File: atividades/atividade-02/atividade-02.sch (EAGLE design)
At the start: 10 parts, among them IC1 LM358N, Q1 BS170

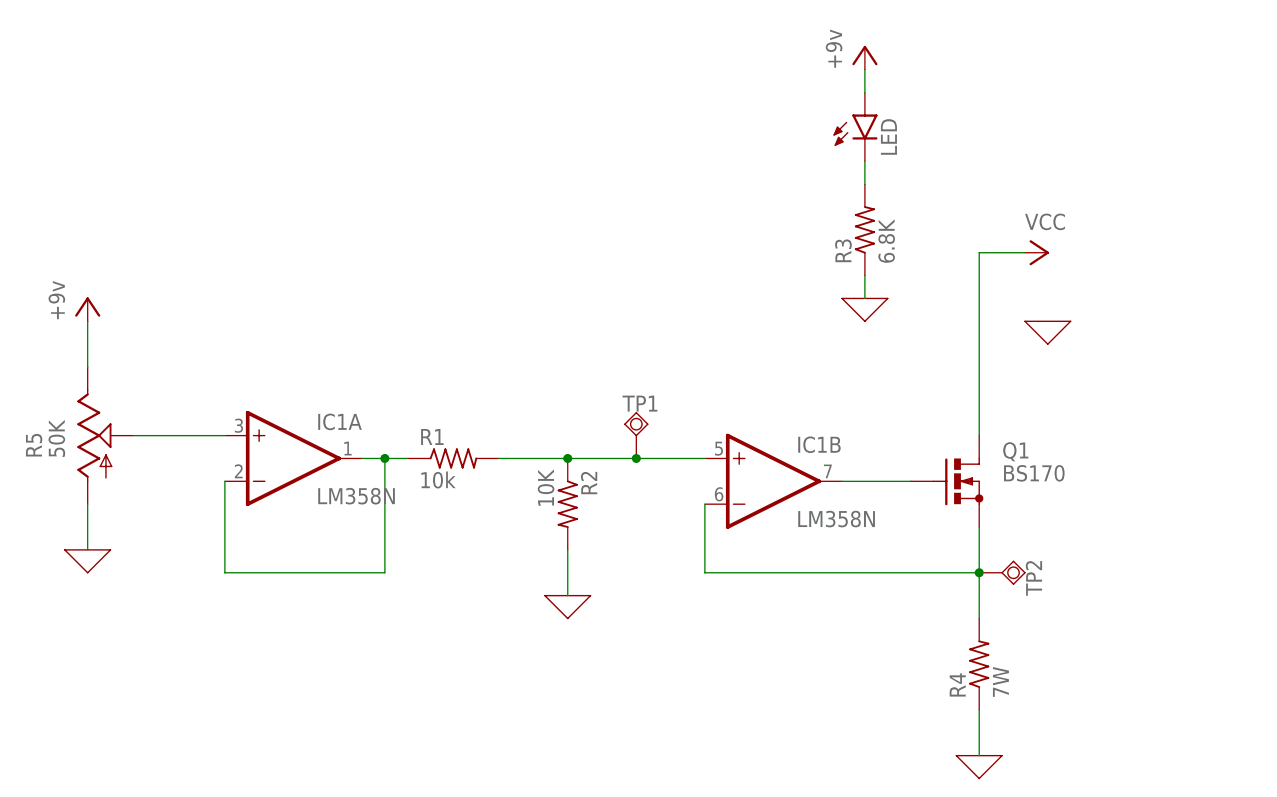
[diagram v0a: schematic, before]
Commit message: renomeando componentes
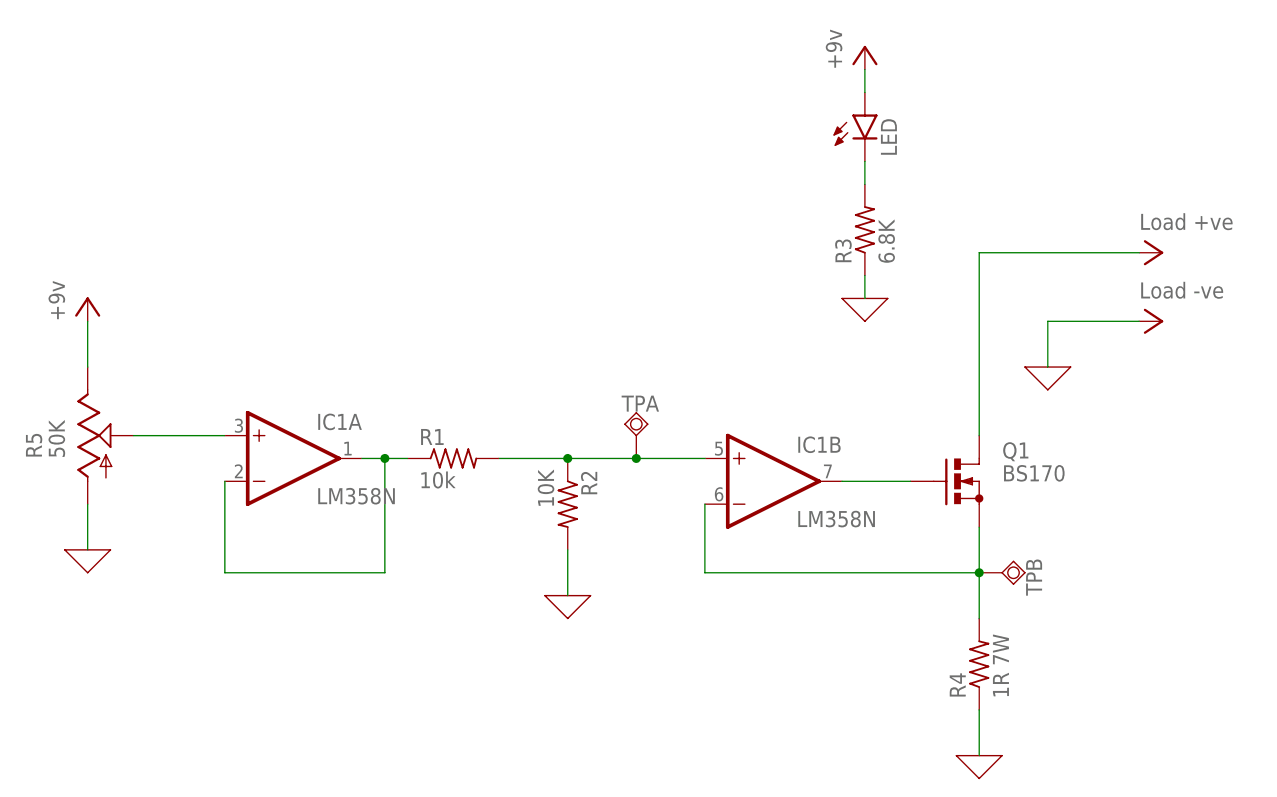
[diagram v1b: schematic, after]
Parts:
- R4: value 7W -> 1R 7W
- renumbered TP1 to TPA, TP2 to TPB
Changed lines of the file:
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@@
 <part name="R3" library="rcl" library_urn="urn:adsk.eagle:library:334" deviceset="R-US_" device="0204/5" package3d_urn="urn:adsk.eagle:package:23488/1" value="6.8K"/>
 <part name="LED" library="led" library_urn="urn:adsk.eagle:library:259" deviceset="LED" device="3MM" package3d_urn="urn:adsk.eagle:package:15797/1"/>
-<part name="P+4" library="supply1" library_urn="urn:adsk.eagle:library:371" deviceset="VCC" device=""/>
+<part name="P+4" library="supply1" library_urn="urn:adsk.eagle:library:371" deviceset="VCC" device="" value="Load +ve"/>
 <part name="X_7" library="ngspice-simulation" library_urn="urn:adsk.eagle:library:527439" deviceset="GND" device=""/>
 <part name="Q1" library="transistor-small-signal" library_urn="urn:adsk.eagle:library:401" deviceset="BS170" device="" package3d_urn="urn:adsk.eagle:package:29751/2"/>
-<part name="TP1" library="testpad" library_urn="urn:adsk.eagle:library:385" deviceset="TPSQ" device="PAD1-20" package3d_urn="urn:adsk.eagle:package:27950/1"/>
-<part name="TP2" library="testpad" library_urn="urn:adsk.eagle:library:385" deviceset="TPSQ" device="PAD1-20" package3d_urn="urn:adsk.eagle:package:27950/1"/>
+<part name="TPA" library="testpad" library_urn="urn:adsk.eagle:library:385" deviceset="TPSQ" device="PAD1-20" package3d_urn="urn:adsk.eagle:package:27950/1"/>
+<part name="TPB" library="testpad" library_urn="urn:adsk.eagle:library:385" deviceset="TPSQ" device="PAD1-20" package3d_urn="urn:adsk.eagle:package:27950/1"/>
 <part name="P+5" library="supply1" library_urn="urn:adsk.eagle:library:371" deviceset="VCC" device="" value="+9v"/>
-<part name="R4" library="rcl" library_urn="urn:adsk.eagle:library:334" deviceset="R-US_" device="0204/5" package3d_urn="urn:adsk.eagle:package:23488/1" value="7W"/>
+<part name="R4" library="rcl" library_urn="urn:adsk.eagle:library:334" deviceset="R-US_" device="0204/5" package3d_urn="urn:adsk.eagle:package:23488/1" value="1R 7W"/>
 <part name="R5" library="pot" library_urn="urn:adsk.eagle:library:331" deviceset="US-EVU" device="M" package3d_urn="urn:adsk.eagle:package:22734/1" technology="F2" value="50K"/>
+<part name="P+2" library="supply1" library_urn="urn:adsk.eagle:library:371" deviceset="VCC" device="" value="Load -ve"/>
 </parts>
 <sheets>
@@
 <attribute name="VALUE" x="102.235" y="109.728" size="1.778" layer="96" rot="R90"/>
 </instance>
-<instance part="P+4" gate="VCC" x="116.84" y="99.06" smashed="yes" rot="R270">
-<attribute name="VALUE" x="114.3" y="101.6" size="1.778" layer="96"/>
+<instance part="P+4" gate="VCC" x="129.54" y="99.06" smashed="yes" rot="R270">
+<attribute name="VALUE" x="127" y="101.6" size="1.778" layer="96"/>
 </instance>
-<instance part="X_7" gate="G$1" x="116.84" y="91.44" smashed="yes"/>
+<instance part="X_7" gate="G$1" x="116.84" y="86.36" smashed="yes"/>
 <instance part="Q1" gate="1" x="106.68" y="73.66" smashed="yes">
 <attribute name="NAME" x="111.76" y="76.2" size="1.778" layer="95"/>
 <attribute name="VALUE" x="111.76" y="73.66" size="1.778" layer="96"/>
 </instance>
-<instance part="TP1" gate="G$1" x="71.12" y="78.74" smashed="yes" rot="R180">
+<instance part="TPA" gate="G$1" x="71.12" y="78.74" smashed="yes" rot="R180">
 <attribute name="NAME" x="73.66" y="83.185" size="1.778" layer="95" rot="R180"/>
 <attribute name="TP_SIGNAL_NAME" x="68.58" y="80.01" size="1.778" layer="97" rot="R180"/>
 </instance>
-<instance part="TP2" gate="G$1" x="111.76" y="63.5" smashed="yes" rot="R90">
+<instance part="TPB" gate="G$1" x="111.76" y="63.5" smashed="yes" rot="R90">
 <attribute name="NAME" x="116.205" y="60.96" size="1.778" layer="95" rot="R90"/>
 <attribute name="TP_SIGNAL_NAME" x="113.03" y="66.04" size="1.778" layer="97" rot="R90"/>
@@
 <attribute name="NAME" x="5.08" y="76.2" size="1.778" layer="95" rot="R90"/>
 <attribute name="VALUE" x="7.62" y="76.2" size="1.778" layer="96" rot="R90"/>
+</instance>
+<instance part="P+2" gate="VCC" x="129.54" y="91.44" smashed="yes" rot="R270">
+<attribute name="VALUE" x="127" y="93.98" size="1.778" layer="96"/>
 </instance>
 </instances>
@@
 <pinref part="P+4" gate="VCC" pin="VCC"/>
 <wire x1="109.22" y1="78.74" x2="109.22" y2="99.06" width="0.1524" layer="91"/>
-<wire x1="109.22" y1="99.06" x2="114.3" y2="99.06" width="0.1524" layer="91"/>
+<wire x1="109.22" y1="99.06" x2="127" y2="99.06" width="0.1524" layer="91"/>
 </segment>
 <segment>
@@
 <pinref part="P+1" gate="VCC" pin="VCC"/>
 <wire x1="10.16" y1="86.36" x2="10.16" y2="91.44" width="0.1524" layer="91"/>
+</segment>
+<segment>
+<pinref part="P+2" gate="VCC" pin="VCC"/>
+<pinref part="X_7" gate="G$1" pin="0"/>
+<wire x1="127" y1="91.44" x2="116.84" y2="91.44" width="0.1524" layer="91"/>
+<wire x1="116.84" y1="91.44" x2="116.84" y2="86.36" width="0.1524" layer="91"/>
 </segment>
 </net>
@@
 <pinref part="R2" gate="G$1" pin="1"/>
 <wire x1="55.88" y1="76.2" x2="63.5" y2="76.2" width="0.1524" layer="91"/>
-<pinref part="TP1" gate="G$1" pin="TP"/>
+<pinref part="TPA" gate="G$1" pin="TP"/>
 <wire x1="63.5" y1="76.2" x2="71.12" y2="76.2" width="0.1524" layer="91"/>
 <junction x="63.5" y="76.2"/>
@@
 <pinref part="IC1" gate="B" pin="-IN"/>
 <wire x1="78.74" y1="71.12" x2="78.74" y2="63.5" width="0.1524" layer="91"/>
-<pinref part="TP2" gate="G$1" pin="TP"/>
+<pinref part="TPB" gate="G$1" pin="TP"/>
 <wire x1="78.74" y1="63.5" x2="109.22" y2="63.5" width="0.1524" layer="91"/>
 <pinref part="Q1" gate="1" pin="S"/>
